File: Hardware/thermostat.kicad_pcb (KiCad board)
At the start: 2 copper layers, 10 parts, among them K1 CONN_3_V, P1 CONN_01X01, P2 CONN_01X01

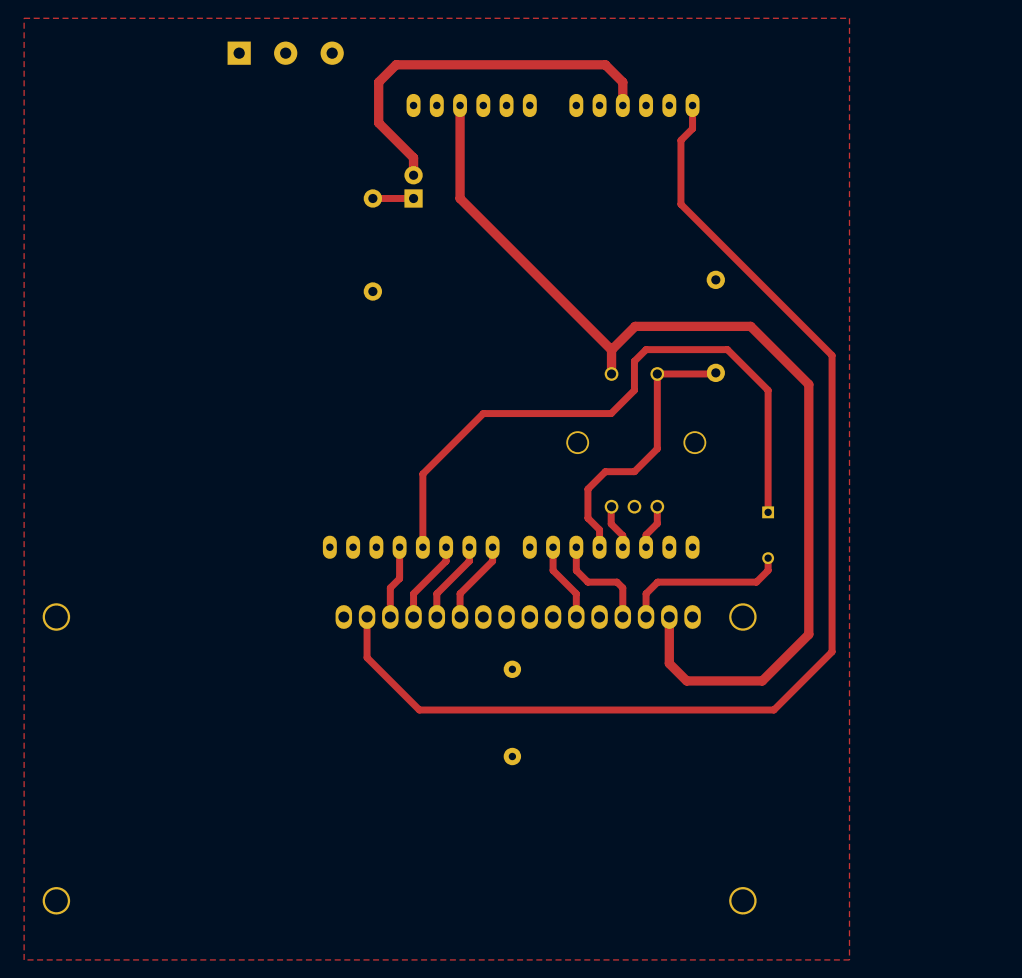
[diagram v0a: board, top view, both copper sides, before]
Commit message: Added headers to improve ground connectivity and added relay and temp&hum headers
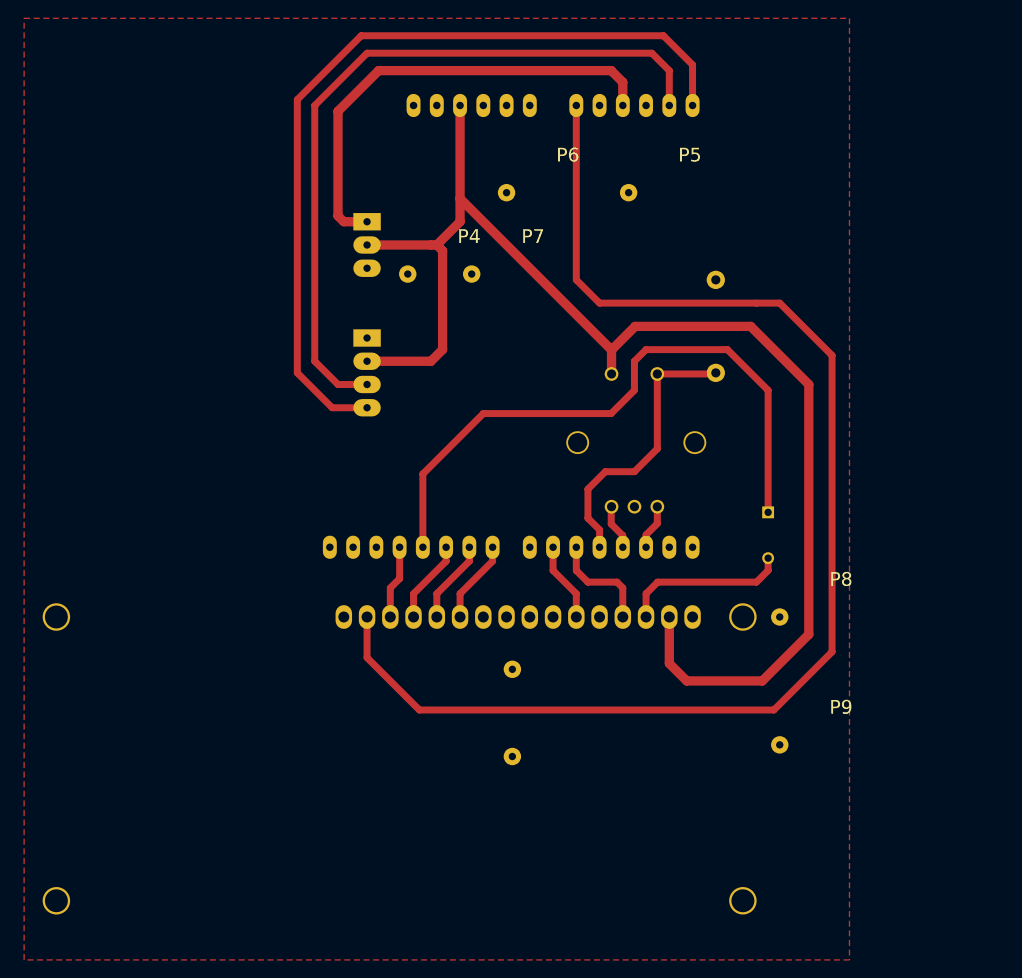
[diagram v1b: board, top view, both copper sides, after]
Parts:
- removed D1: LED, LEDs:LED-3MM
- removed K1: CONN_3_V, borniers:bornier3_V
- added P3: CONN_01X04 (T&H), Pin_Headers:Pin_Header_Angled_1x04, B.Cu at (52.1, 78.7)
- added P4: CONN_01X01, library:header1x01, F.Cu at (56.5, 71.8)
- added P5: CONN_01X01, library:header1x01, F.Cu at (80.6, 62.9)
- added P6: CONN_01X01, library:header1x01, F.Cu at (67.3, 62.9)
- added P7: CONN_01X01, library:header1x01, F.Cu at (63.5, 71.8)
- added P8: CONN_01X01, library:header1x01, F.Cu at (97.2, 109.2)
- added P9: CONN_01X01, library:header1x01, F.Cu at (97.2, 123.2)
- R1: value 10K -> relay_module; footprint Resistors_ThroughHole:Resistor_Horizontal_RM10mm -> Pin_Headers:Pin_Header_Angled_1x03
- moved R1 2.62 mm to (52.1, 66.0), turned to 180 degrees
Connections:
- R1 pad 1: GND -> RELAY
- R1 pad 2: Net-(D1-Pad1) -> VCC
- SHIELD1 pad AD0: Net-(SHIELD1-PadAD0) -> BKL
- SHIELD1 pad AD4: Net-(SHIELD1-PadAD4) -> SDA
- SHIELD1 pad AD5: BKL -> SCL
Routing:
- net SCL: track 0.00 -> 90.9 mm
- net SDA: track 0.00 -> 80.4 mm
- net VCC: track 112.0 -> 146.2 mm
- net BKL: track 127.3 -> 143.0 mm
- net RELAY: track 42.5 -> 50.9 mm
- net Net-(D1-Pad1): track 4.45 -> 0.00 mm

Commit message: Added 3 pin header for analog device, decrease pcb size
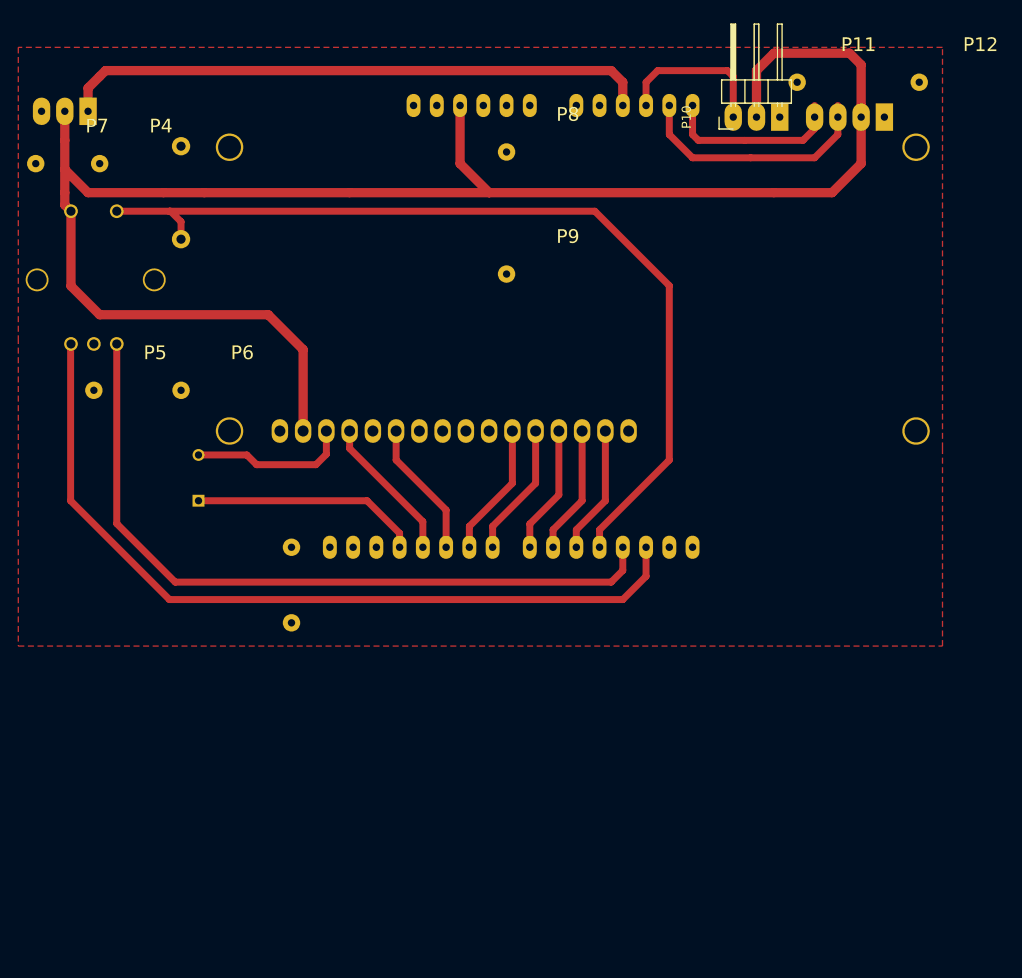
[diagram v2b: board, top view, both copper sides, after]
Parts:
- added P10: CONN_01X03, Pin_Headers:Pin_Header_Angled_1x03, F.Cu at (92.1, 54.6)
- added P11: CONN_01X01, library:header1x01, F.Cu at (99.1, 50.8)
- added P12: CONN_01X01, library:header1x01, F.Cu at (112.4, 50.8)
- moved P5 62.3 mm to (22.2, 84.5)
- moved C1 62.2 mm to (33.7, 96.5), turned to 90 degrees
- moved EN1 61.7 mm to (22.2, 72.4)
- moved P3 61.5 mm to (108.6, 54.6), turned to 90 degrees
- moved R2 60.2 mm to (31.8, 62.9)
- moved P9 59.5 mm to (67.3, 71.8)
- moved P8 58.9 mm to (67.3, 58.4)
- moved DS1 49.5 mm to (42.5, 88.9), turned to 0 degrees
- moved P7 49.1 mm to (15.9, 59.7)
- moved P6 41.6 mm to (31.8, 84.5)
- moved P4 35.8 mm to (22.9, 59.7)
- moved R1 32.8 mm to (21.6, 54.0), turned to 90 degrees
- moved P2 28.2 mm to (43.8, 109.9)
- moved P1 27.6 mm to (43.8, 101.6)
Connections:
- SHIELD1 pad 10: D6 -> E
- SHIELD1 pad 11: V0 -> RS
- SHIELD1 pad 12: D7 -> V0
- SHIELD1 pad 2: Net-(EN1-Pad1) -> Net-(EN1-Pad3)
- SHIELD1 pad 3: Net-(EN1-Pad3) -> Net-(EN1-Pad1)
- SHIELD1 pad 5: RS -> BKL
- SHIELD1 pad 6: E -> D7
- SHIELD1 pad 7: Net-(SHIELD1-Pad7) -> D6
- SHIELD1 pad 8: D4 -> D5
- SHIELD1 pad 9: D5 -> D4
- SHIELD1 pad AD0: BKL -> Net-(SHIELD1-PadAD0)
- SHIELD1 pad AD3: Net-(SHIELD1-PadAD3) -> SGN
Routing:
- net BKL: track 143.0 -> 14.0 mm
- net Net-(EN1-Pad3): track 4.97 -> 88.7 mm
- net Net-(EN1-Pad1): track 4.94 -> 80.6 mm
- net SCL: track 90.9 -> 19.8 mm
- net BTN: track 30.9 -> 99.1 mm
- net SDA: track 80.4 -> 26.9 mm
- net V0: track 68.4 -> 25.0 mm
- net VCC: track 146.2 -> 184.0 mm
- net SGN: track 0.00 -> 16.0 mm
- net RELAY: track 50.9 -> 64.8 mm
- net E: track 8.67 -> 15.0 mm
- net D7: track 8.04 -> 14.0 mm
- net D4: track 9.09 -> 15.0 mm
- net D5: track 9.45 -> 14.6 mm
- net D6: track 9.09 -> 14.0 mm
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
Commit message: improved pads
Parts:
- P10: moved to B.Cu
- moved P10 5.08 mm to (97.2, 54.6)
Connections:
- P10 pad 1: SGN -> GND
- P10 pad 3: GND -> SGN
